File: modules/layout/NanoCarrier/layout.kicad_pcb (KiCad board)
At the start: 4 copper layers, 19 x 44 mm, 36 parts, among them IC1 ATMEGA328PMAU, IC2 AMS1117M5_0, IC3 FT231XQMR, J1 2.54mm 15x1, J2 2.54mm 15x1, J3 10033526MN3212LF, J4 2.54mm 3x2, Y1 16MHz 18pF

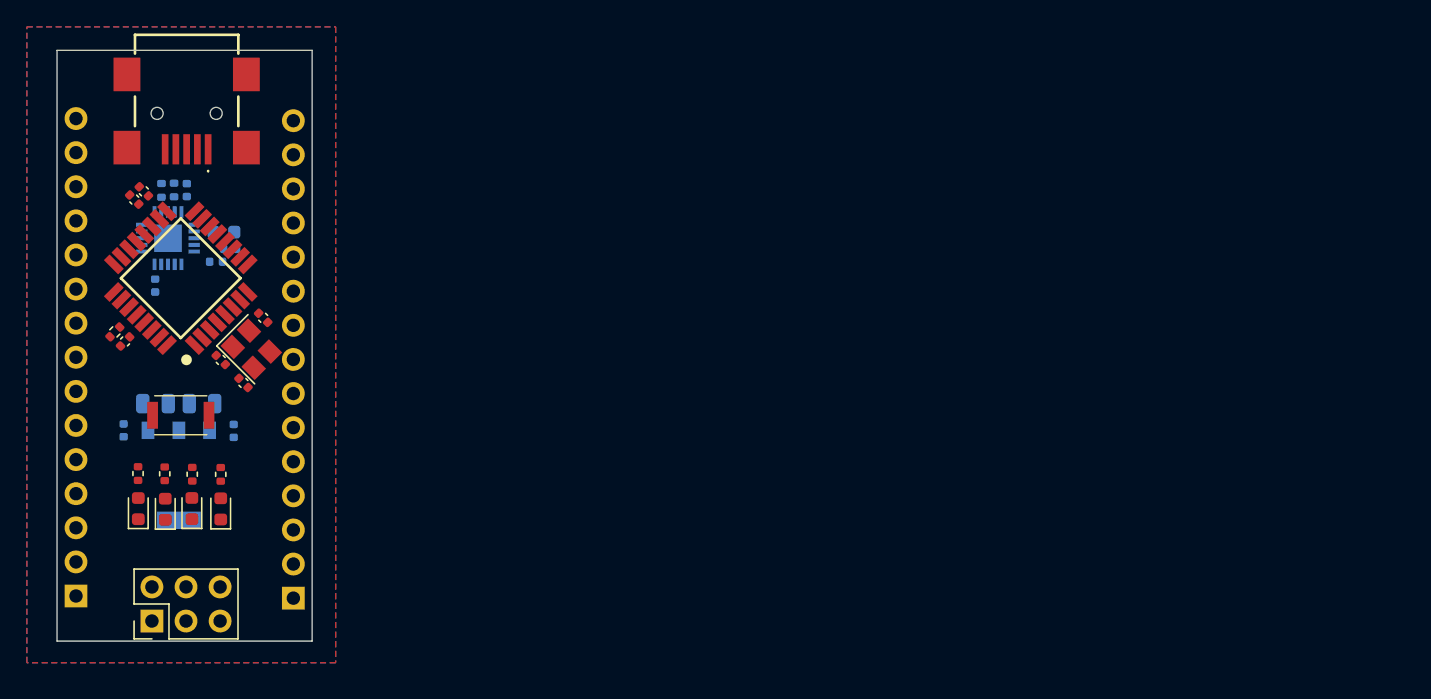
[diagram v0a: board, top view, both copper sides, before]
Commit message: use carrier and core arch
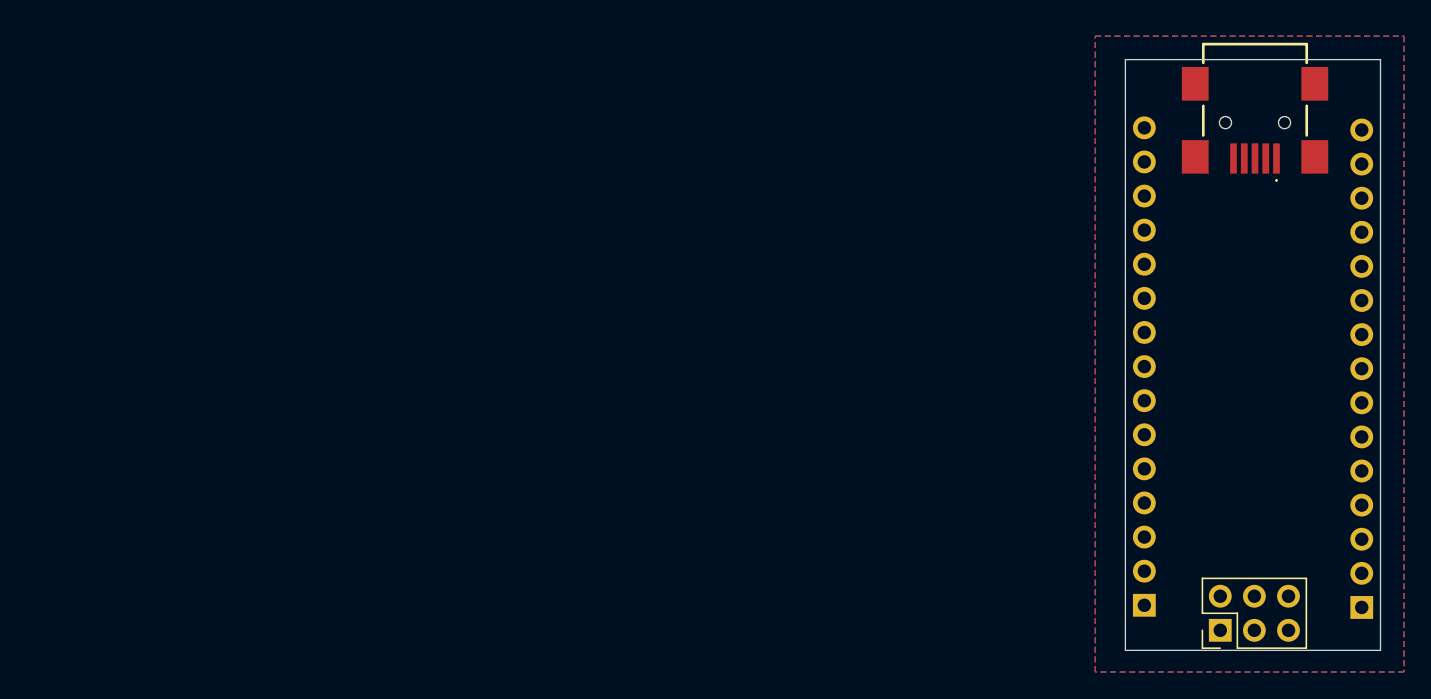
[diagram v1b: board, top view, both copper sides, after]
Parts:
- removed C1: 100nF, C_0402_1005Metric:C_0402_1005Metric
- removed C10, C12, C13, C14: 100nF 10V, C_0402_1005Metric:C_0402_1005Metric
- removed C11, C2, C3, C4: 100nF 6.3V, C_0402_1005Metric:C_0402_1005Metric
- removed C15: 4.7uF 10V, C_0603_1608Metric:C_0603_1608Metric
- removed C5, C6: 22pF C0G, C_0402_1005Metric:C_0402_1005Metric
- removed C7: 10uF 25V, C_0805_2012Metric:C_0805_2012Metric
- removed C8: 100nF 25V, C_0402_1005Metric:C_0402_1005Metric
- removed C9: 22uF 10V, C_0805_2012Metric:C_0805_2012Metric
- removed D1: LED YELLOW, LED_0603_1608Metric:LED_0603_1608Metric
- removed D2, D3, D4: LED GREEN, LED_0603_1608Metric:LED_0603_1608Metric
- removed IC1: ATMEGA328PMAU, QFP80P900X900X120-32N:QFP80P900X900X120-32N
- removed IC2: AMS1117M5_0, SOT229P700X180-4N:SOT229P700X180-4N
- removed IC3: FT231XQMR, QFN50P400X400X80-21N:QFN50P400X400X80-21N
- removed R1: 10k 5%, R_0402_1005Metric:R_0402_1005Metric
- removed R2, R3: 1k 5%, R_0402_1005Metric:R_0402_1005Metric
- removed R4, R5: 470 5%, R_0402_1005Metric:R_0402_1005Metric
- removed R6, R7: 27 5%, R_0402_1005Metric:R_0402_1005Metric
- removed S1: SKRKAHE020, SKRKAEE020:SKRKAEE020
- removed V1: ?, version-footprint:version-footprint
- removed Y1: 16MHz 18pF, Crystal_SMD_3225-4Pin_3.2x2.5mm:Crystal_SMD_3225-4Pin_3.2x2.5mm
- moved J2 79.6 mm to (143.1, 122.1)
- moved J4 79.6 mm to (148.8, 124.0)
- moved J1 79.6 mm to (159.3, 122.3)
- moved J3 79.6 mm to (151.4, 84.9)
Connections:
- net NANO_CARRIER.NC renamed NC
- net NANO_CARRIER.NC_2 renamed NC_2
- net USB_DATA_D_N renamed USB_D_N
- net USB_DATA_D_P renamed USB_D_P
- J1 pad 1: UART_RX -> D0
- J1 pad 4: UART_TX -> D1
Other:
- board text removed: "0"
- board text removed: "0 mm"
- board text removed: "0.01 mm"
- board text removed: "0.0152 mm"
- board text removed: "0.025"
- board text removed: "0.035 mm"
- board text removed: "0.0900 mm / 0.0900 mm"
- board text removed: "0.1500 mm"
- board text removed: "0.2104 mm"
- board text removed: "1"
- board text removed: "1.065 mm"
- board text removed: "1.6062 mm"
- board text removed: "19.0000 mm x 44.0000 mm"
- board text removed: "3.3"
- board text removed: "4"
- board text removed: "4.4"
- board text removed: "4.6"
- board text removed: "B.Cu"
- board text removed: "B.Mask"
- board text removed: "B.Paste"
- board text removed: "B.Silkscreen"
- board text removed: "BOARD CHARACTERISTICS"
- board text removed: "Blue"
- board text removed: "Board Thickness:"
- board text removed: "Board overall dimensions:"
- board text removed: "Bottom Silk Screen"
- board text removed: "Bottom Solder Mask"
- board text removed: "Bottom Solder Paste"
- board text removed: "Castellated pads:"
- board text removed: "Color"
- board text removed: "Copper Finish:"
- board text removed: "Copper Layer Count:"
- board text removed: "Dielectric"
- board text removed: "ENIG"
- board text removed: "Edge card connectors:"
- board text removed: "Epsilon R"
- board text removed: "F.Cu"
- board text removed: "F.Mask"
- board text removed: "F.Paste"
- board text removed: "F.Silkscreen"
- board text removed: "FR4-Core"
- board text removed: "Impedance Control:"
- board text removed: "In1.Cu"
- board text removed: "In2.Cu"
- board text removed: "Layer Name"
- board text removed: "Loss Tangent"
- board text removed: "Material"
- board text removed: "Min hole diameter:"
- board text removed: "Min track/spacing:"
- board text removed: "No"
- board text removed: "Not specified"
- board text removed: "Plated Board Edge:"
- board text removed: "Prepreg"
- board text removed: "Thickness (mm)"
- board text removed: "Top Silk Screen"
- board text removed: "Top Solder Mask"
- board text removed: "Top Solder Paste"
- board text removed: "Type"
- board text removed: "White"
- board text removed: "copper"
- board text removed: "core"
- board text removed: "prepreg"
